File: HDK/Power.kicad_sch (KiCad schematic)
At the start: 1 part, among them U201 AMS1117

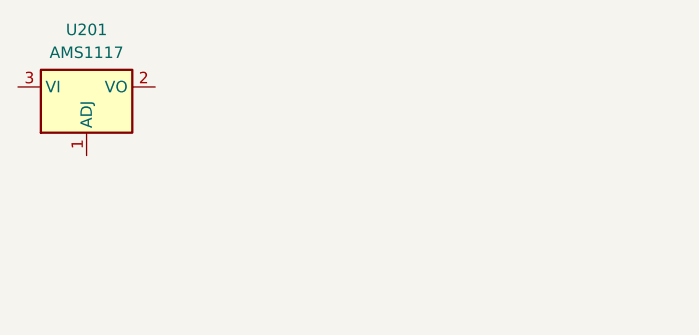
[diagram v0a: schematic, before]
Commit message: trying out nested schs
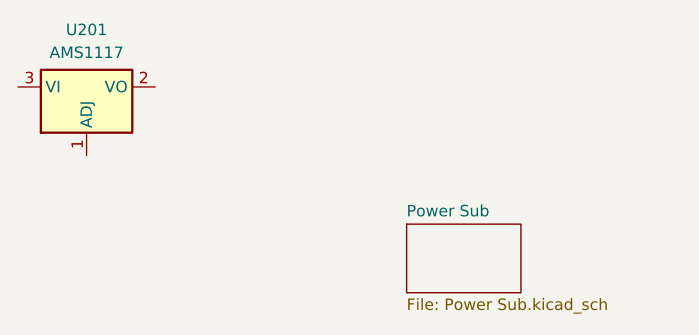
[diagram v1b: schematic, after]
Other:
- added sheet Power Sub (Power Sub.kicad_sch)
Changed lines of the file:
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@@
+		)
+	)
+	(sheet
+		(at 123.19 67.31)
+		(size 12.7 7.62)
+		(fields_autoplaced yes)
+		(stroke
+			(width 0.1524)
+			(type solid)
+		)
+		(fill
+			(color 0 0 0 0.0000)
+		)
+		(property "Sheetname" "Power Sub"
+			(at 123.19 66.5984 0)
+			(effects
+				(font
+					(size 1.27 1.27)
+				)
+				(justify left bottom)
+			)
+		)
+		(property "Sheetfile" "Power Sub.kicad_sch"
+			(at 123.19 75.5146 0)
+			(effects
+				(font
+					(size 1.27 1.27)
+				)
+				(justify left top)
+			)
+		)
+		(instances
+			(project "template_project"
+				(path "/26f9cb6a-983b-4cfb-90f4-253f3e225603/5a8acf05-2a27-44a5-a288-e5d9b346ca3c"
+					(page "3")
+				)
+			)
 		)
 	)
